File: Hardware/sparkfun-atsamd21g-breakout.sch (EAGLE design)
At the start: 41 parts, among them Q1 2N7002PW, Q3 2.5A/30V, U1 ATSAMD21G-A, U2 MIC5219 3.3V, U3 74AHC1G125, Y1 32.768kHz

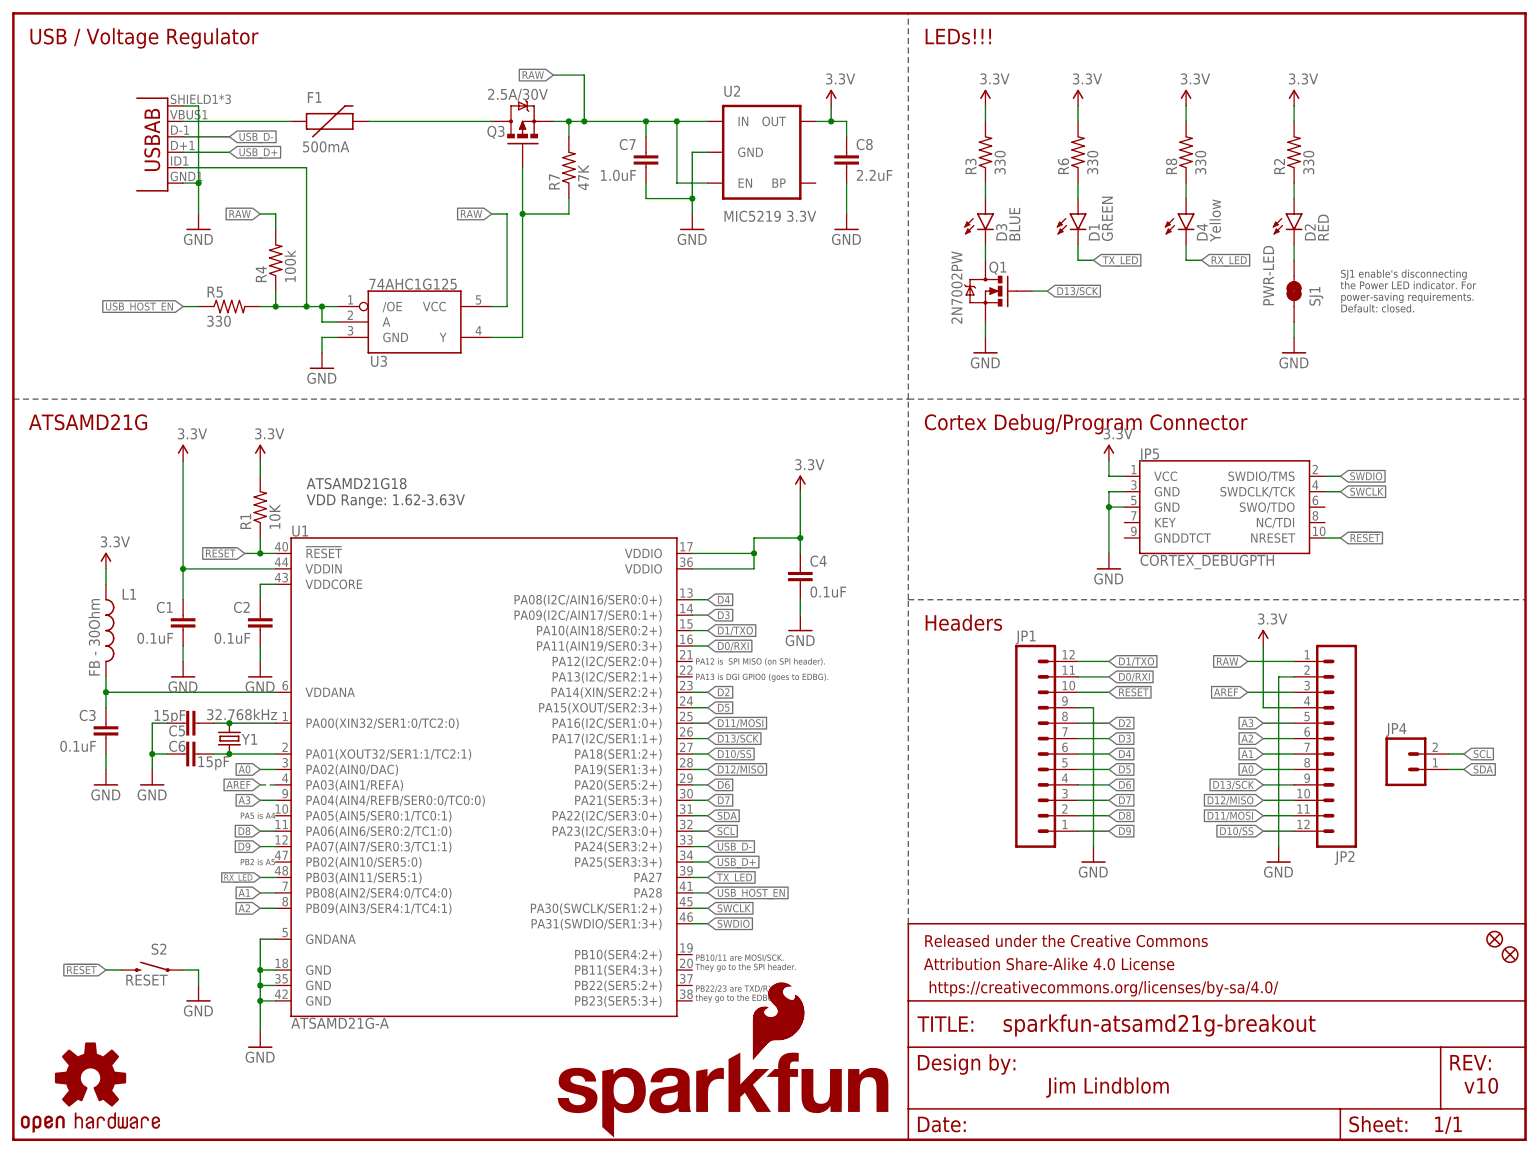
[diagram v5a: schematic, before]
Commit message: Swapping MIC5205 Regulator out for AP2112K-3.3V
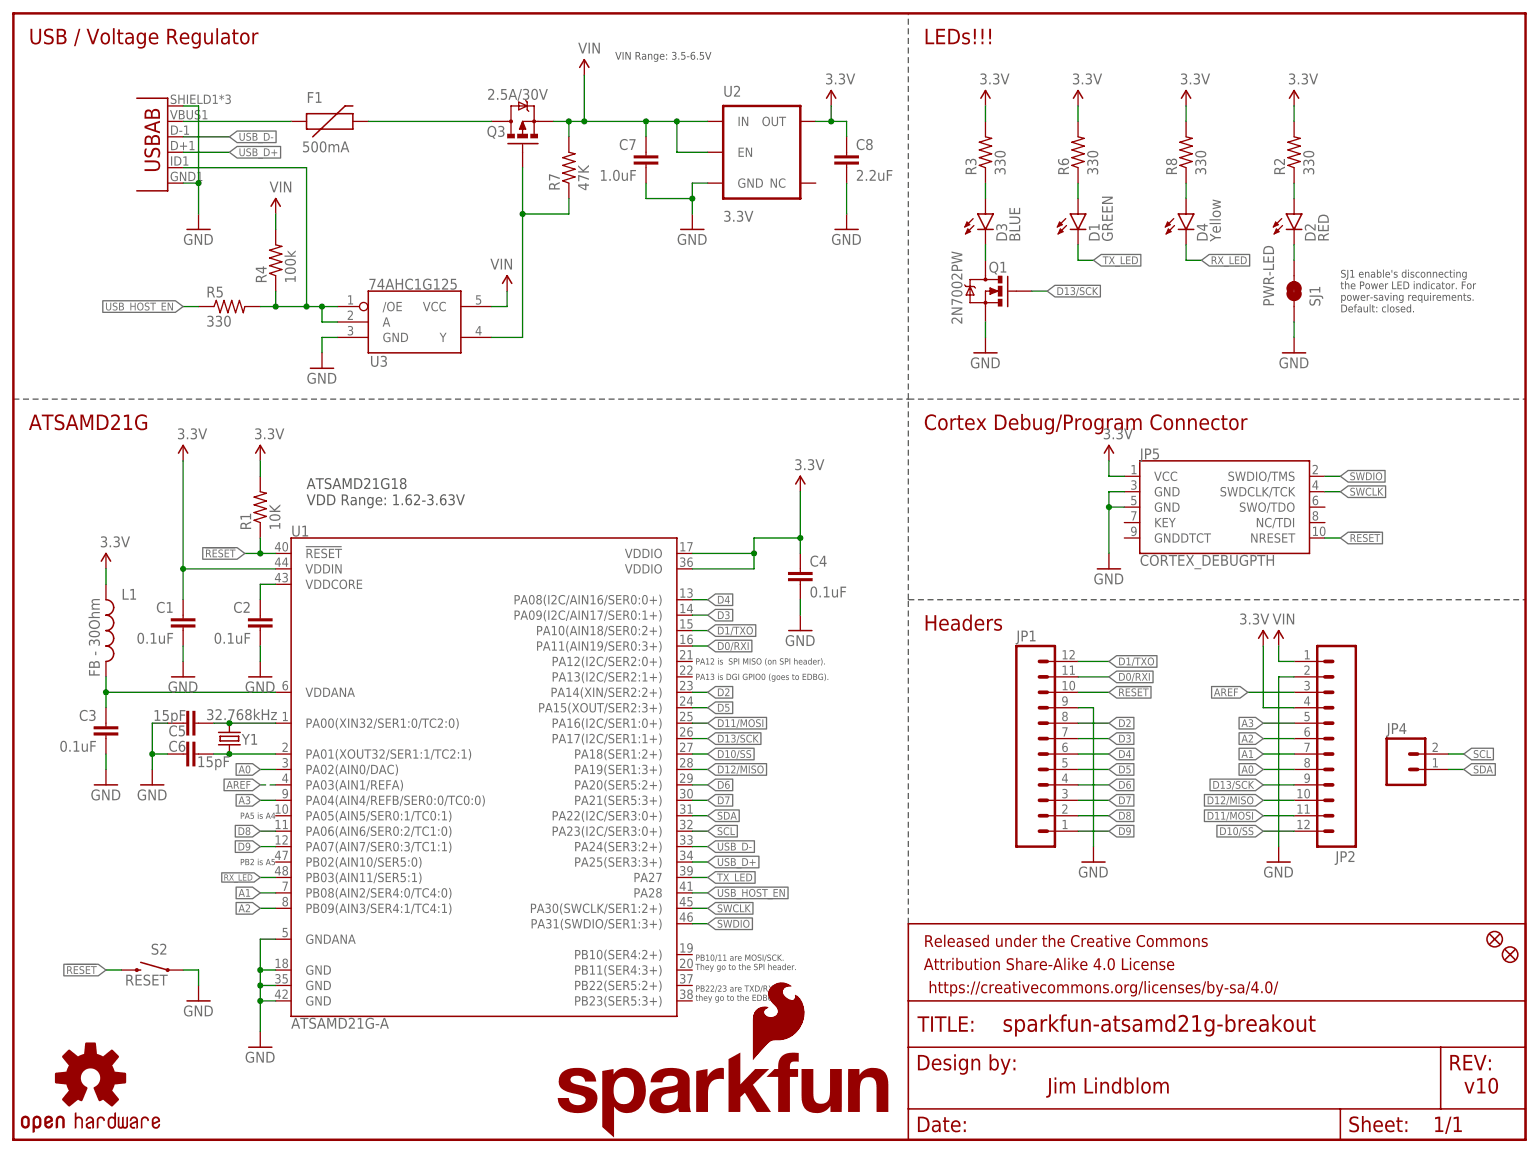
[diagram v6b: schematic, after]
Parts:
- U2: value MIC5219 3.3V -> 3.3V; device SparkFun-PowerIC:V_REG_MIC52193.3V -> SparkFun-PowerIC:V_REG_AP2112K-3.3V
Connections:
- net RAW renamed VIN
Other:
- note added: "VIN Range: 3.5-6.5V"
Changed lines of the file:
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@@
 <part name="GND8" library="SparkFun-Aesthetics" deviceset="GND" device=""/>
 <part name="GND9" library="SparkFun-Aesthetics" deviceset="GND" device=""/>
-<part name="U2" library="SparkFun-PowerIC" deviceset="V_REG_MIC5219" device="3.3V" value="MIC5219 3.3V"/>
+<part name="U2" library="SparkFun-PowerIC" deviceset="V_REG_AP2112" device="K-3.3V" value="3.3V"/>
 <part name="GND10" library="SparkFun-Aesthetics" deviceset="GND" device=""/>
 <part name="GND11" library="SparkFun-Aesthetics" deviceset="GND" device=""/>
@@
 <part name="FID1" library="SparkFun-Aesthetics" deviceset="FIDUCIAL" device="1X2"/>
 <part name="FID2" library="SparkFun-Aesthetics" deviceset="FIDUCIAL" device="1X2"/>
+<part name="SUPPLY10" library="SparkFun-Aesthetics" deviceset="VIN" device=""/>
+<part name="SUPPLY11" library="SparkFun-Aesthetics" deviceset="VIN" device=""/>
+<part name="SUPPLY14" library="SparkFun-Aesthetics" deviceset="VIN" device=""/>
+<part name="SUPPLY15" library="SparkFun-Aesthetics" deviceset="VIN" device=""/>
 </parts>
 <sheets>
@@
 power-saving requirements.
 Default: closed.</text>
+<text x="99.06" y="177.8" size="1.27" layer="97">VIN Range: 3.5-6.5V</text>
 </plain>
 <instances>
@@
 <instance part="GND15" gate="1" x="160.02" y="129.54"/>
 <instance part="D3" gate="G$1" x="160.02" y="152.4"/>
-<instance part="SUPPLY7" gate="G$1" x="205.74" y="81.28"/>
+<instance part="SUPPLY7" gate="G$1" x="205.74" y="81.28" rot="MR0"/>
 <instance part="C7" gate="G$1" x="104.14" y="160.02" rot="MR0"/>
 <instance part="C8" gate="G$1" x="137.16" y="160.02"/>
@@
 <instance part="FID1" gate="G$1" x="246.38" y="30.48"/>
 <instance part="FID2" gate="G$1" x="243.84" y="33.02"/>
+<instance part="SUPPLY10" gate="G$1" x="43.18" y="152.4"/>
+<instance part="SUPPLY11" gate="G$1" x="81.28" y="139.7" rot="MR0"/>
+<instance part="SUPPLY14" gate="G$1" x="93.98" y="175.26"/>
+<instance part="SUPPLY15" gate="G$1" x="208.28" y="81.28"/>
 </instances>
 <busses>
@@
 <pinref part="U2" gate="G$1" pin="GND"/>
 <pinref part="GND10" gate="1" pin="GND"/>
-<wire x1="114.3" y1="162.56" x2="111.76" y2="162.56" width="0.1524" layer="91"/>
-<wire x1="111.76" y1="162.56" x2="111.76" y2="154.94" width="0.1524" layer="91"/>
+<wire x1="114.3" y1="157.48" x2="111.76" y2="157.48" width="0.1524" layer="91"/>
+<wire x1="111.76" y1="157.48" x2="111.76" y2="154.94" width="0.1524" layer="91"/>
 <wire x1="111.76" y1="154.94" x2="111.76" y2="152.4" width="0.1524" layer="91"/>
 <wire x1="104.14" y1="157.48" x2="104.14" y2="154.94" width="0.1524" layer="91"/>
@@
 </segment>
 </net>
-<net name="RAW" class="0">
+<net name="VIN" class="0">
 <segment>
 <pinref part="JP2" gate="G$1" pin="1"/>
-<wire x1="210.82" y1="78.74" x2="203.2" y2="78.74" width="0.1524" layer="91"/>
-<label x="203.2" y="78.74" size="1.27" layer="95" rot="R180" xref="yes"/>
+<wire x1="210.82" y1="78.74" x2="208.28" y2="78.74" width="0.1524" layer="91"/>
+<pinref part="SUPPLY15" gate="G$1" pin="VIN"/>
+<wire x1="208.28" y1="78.74" x2="208.28" y2="81.28" width="0.1524" layer="91"/>
 </segment>
 <segment>
@@
 <junction x="104.14" y="167.64"/>
 <pinref part="U2" gate="G$1" pin="EN"/>
-<wire x1="114.3" y1="157.48" x2="109.22" y2="157.48" width="0.1524" layer="91"/>
-<wire x1="109.22" y1="157.48" x2="109.22" y2="167.64" width="0.1524" layer="91"/>
+<wire x1="114.3" y1="162.56" x2="109.22" y2="162.56" width="0.1524" layer="91"/>
+<wire x1="109.22" y1="162.56" x2="109.22" y2="167.64" width="0.1524" layer="91"/>
 <junction x="109.22" y="167.64"/>
 <wire x1="93.98" y1="167.64" x2="104.14" y2="167.64" width="0.1524" layer="91"/>
 <wire x1="93.98" y1="167.64" x2="93.98" y2="175.26" width="0.1524" layer="91"/>
 <junction x="93.98" y="167.64"/>
-<wire x1="93.98" y1="175.26" x2="88.9" y2="175.26" width="0.1524" layer="91"/>
-<label x="88.9" y="175.26" size="1.27" layer="95" rot="R180" xref="yes"/>
 <pinref part="C7" gate="G$1" pin="1"/>
 <pinref part="Q3" gate="G$1" pin="S"/>
@@
 <junction x="91.44" y="167.64"/>
 <pinref part="R7" gate="G$1" pin="2"/>
+<pinref part="SUPPLY14" gate="G$1" pin="VIN"/>
 </segment>
 <segment>
 <pinref part="U3" gate="G$1" pin="VCC"/>
 <wire x1="78.74" y1="137.16" x2="81.28" y2="137.16" width="0.1524" layer="91"/>
-<wire x1="81.28" y1="137.16" x2="81.28" y2="152.4" width="0.1524" layer="91"/>
-<label x="78.74" y="152.4" size="1.27" layer="95" rot="R180" xref="yes"/>
-<wire x1="81.28" y1="152.4" x2="78.74" y2="152.4" width="0.1524" layer="91"/>
+<wire x1="81.28" y1="137.16" x2="81.28" y2="139.7" width="0.1524" layer="91"/>
+<pinref part="SUPPLY11" gate="G$1" pin="VIN"/>
 </segment>
 <segment>
 <pinref part="R4" gate="G$1" pin="2"/>
 <wire x1="43.18" y1="149.86" x2="43.18" y2="152.4" width="0.1524" layer="91"/>
-<wire x1="43.18" y1="152.4" x2="40.64" y2="152.4" width="0.1524" layer="91"/>
-<label x="40.64" y="152.4" size="1.27" layer="95" rot="R180" xref="yes"/>
-</segment>
-</net>
+<pinref part="SUPPLY10" gate="G$1" pin="VIN"/>
+</segment>
+</net>

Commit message: Tweaking schematic and layout silk for checklist
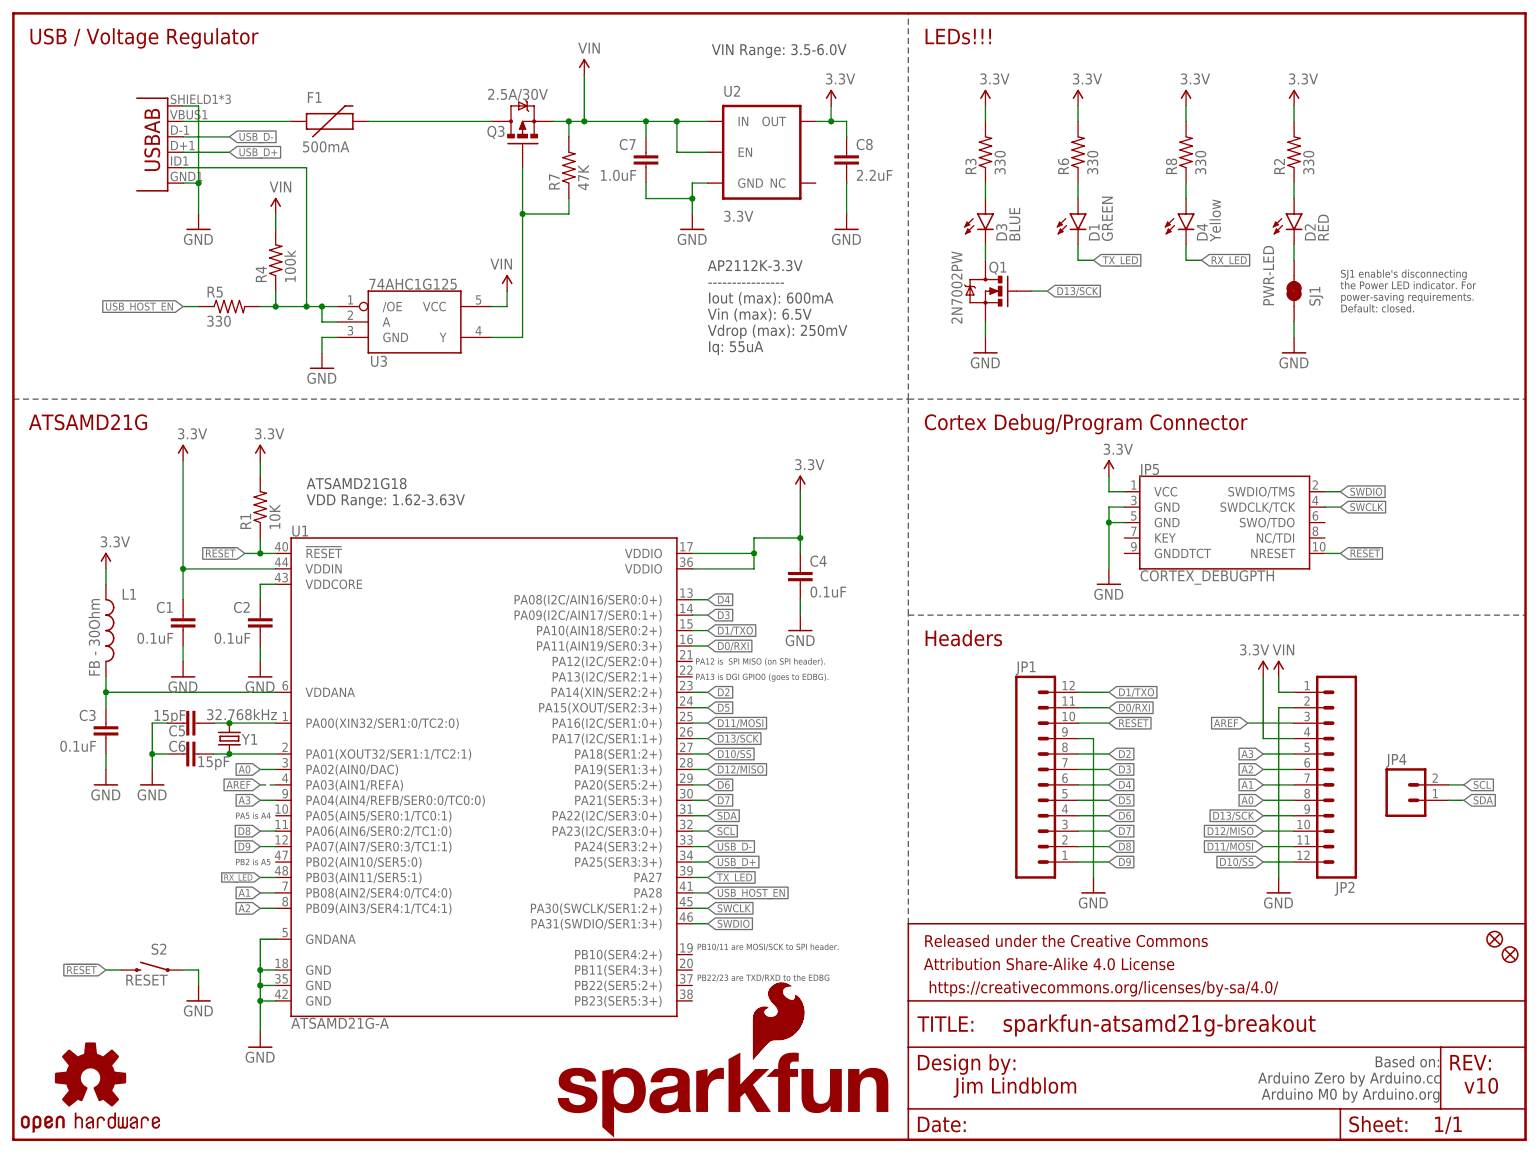
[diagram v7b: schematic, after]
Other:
- note added: "AP2112K-3.3V ---------------- Iout (max): 600mA Vin (max): 6.5V Vdrop (max): 250mV Iq: 55uA"
- note added: "Based on: Arduino Zero by Arduino.cc Arduino M0 by Arduino.org"
- note added: "PB10/11 are MOSI/SCK to SPI header."
- note added: "PB22/23 are TXD/RXD to the EDBG"
- note added: "VIN Range: 3.5-6.0V"
- note removed: "PB10/11 are MOSI/SCK. They go to the SPI header."
- note removed: "PB22/23 are TXD/RXD - they go to the EDBG"
- note removed: "VIN Range: 3.5-6.5V"
- moved on the sheet: JP1, JP2, JP4, JP5

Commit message: Sequentiallizing part names
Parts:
- renumbered Q3 to Q2, S2 to S1
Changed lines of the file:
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@@
 <part name="GND7" library="SparkFun-Aesthetics" deviceset="GND" device=""/>
 <part name="R5" library="SparkFun-Resistors" deviceset="330OHM1/10W1%(0603)" device="" value="330"/>
-<part name="Q3" library="SparkFun-DiscreteSemi" deviceset="MOSFET-PCHANNEL" device="DMG2307L" value="2.5A/30V"/>
+<part name="Q2" library="SparkFun-DiscreteSemi" deviceset="MOSFET-PCHANNEL" device="DMG2307L" value="2.5A/30V"/>
 <part name="R7" library="SparkFun-Resistors" deviceset="47KOHM1/10W1%(0603)" device="" value="47K"/>
 <part name="D1" library="SparkFun-LED" deviceset="LED-GREEN" device="0603" value="GREEN"/>
@@
 <part name="FRAME1" library="SparkFun-Aesthetics" deviceset="FRAME-LETTER" device=""/>
 <part name="SJ1" library="SparkFun-Passives" deviceset="JUMPER-PAD-2-NC_BY_TRACE" device="NO_SILK" value="PWR-LED"/>
-<part name="S2" library="samd21-temp" deviceset="SWITCH-MOMENTARY-2" device="SMD-4.6X2.8MM" value="RESET"/>
+<part name="S1" library="samd21-temp" deviceset="SWITCH-MOMENTARY-2" device="SMD-4.6X2.8MM" value="RESET"/>
 <part name="FID1" library="SparkFun-Aesthetics" deviceset="FIDUCIAL" device="1X2"/>
 <part name="FID2" library="SparkFun-Aesthetics" deviceset="FIDUCIAL" device="1X2"/>
@@
 <instance part="GND7" gate="1" x="50.8" y="127"/>
 <instance part="R5" gate="G$1" x="35.56" y="137.16"/>
-<instance part="Q3" gate="G$1" x="83.82" y="167.64" smashed="yes" rot="R90">
+<instance part="Q2" gate="G$1" x="83.82" y="167.64" smashed="yes" rot="R90">
 <attribute name="NAME" x="81.026" y="166.878" size="1.778" layer="95" rot="R180"/>
 <attribute name="VALUE" x="77.978" y="171.196" size="1.778" layer="96"/>
@@
 <instance part="FRAME1" gate="V" x="147.32" y="0"/>
 <instance part="SJ1" gate="G$1" x="210.82" y="139.7" rot="MR90"/>
-<instance part="S2" gate="G$1" x="22.86" y="27.94" rot="MR0"/>
+<instance part="S1" gate="G$1" x="22.86" y="27.94" rot="MR0"/>
 <instance part="FID1" gate="G$1" x="246.38" y="30.48"/>
 <instance part="FID2" gate="G$1" x="243.84" y="33.02"/>
@@
 <wire x1="30.48" y1="27.94" x2="30.48" y2="25.4" width="0.1524" layer="91"/>
 <pinref part="GND9" gate="1" pin="GND"/>
-<pinref part="S2" gate="G$1" pin="1"/>
+<pinref part="S1" gate="G$1" pin="1"/>
 </segment>
 <segment>
@@
 <wire x1="17.78" y1="27.94" x2="15.24" y2="27.94" width="0.1524" layer="91"/>
 <label x="15.24" y="27.94" size="1.27" layer="95" rot="R180" xref="yes"/>
-<pinref part="S2" gate="G$1" pin="2"/>
+<pinref part="S1" gate="G$1" pin="2"/>
 </segment>
 <segment>
@@
 <junction x="93.98" y="167.64"/>
 <pinref part="C7" gate="G$1" pin="1"/>
-<pinref part="Q3" gate="G$1" pin="S"/>
+<pinref part="Q2" gate="G$1" pin="S"/>
 <wire x1="88.9" y1="167.64" x2="91.44" y2="167.64" width="0.1524" layer="91"/>
 <wire x1="91.44" y1="167.64" x2="91.44" y2="165.1" width="0.1524" layer="91"/>
@@
 <segment>
 <pinref part="F1" gate="G$1" pin="2"/>
-<pinref part="Q3" gate="G$1" pin="D"/>
+<pinref part="Q2" gate="G$1" pin="D"/>
 <wire x1="58.42" y1="167.64" x2="78.74" y2="167.64" width="0.1524" layer="91"/>
 </segment>
@@
 <segment>
 <pinref part="U3" gate="G$1" pin="Y"/>
-<pinref part="Q3" gate="G$1" pin="G"/>
+<pinref part="Q2" gate="G$1" pin="G"/>
 <wire x1="78.74" y1="132.08" x2="83.82" y2="132.08" width="0.1524" layer="91"/>
 <wire x1="83.82" y1="132.08" x2="83.82" y2="152.4" width="0.1524" layer="91"/>
